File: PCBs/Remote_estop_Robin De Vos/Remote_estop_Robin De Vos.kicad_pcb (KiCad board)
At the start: 2 copper layers, 52 x 43.5 mm, 22 parts, among them J1 UART connector, J2 USB_B_Micro, SW1 SW_Push, SW2 SW_Push, SW3 SW_Push, U1 ESP32-WROOM-32E, U2 AMS1117-3.3

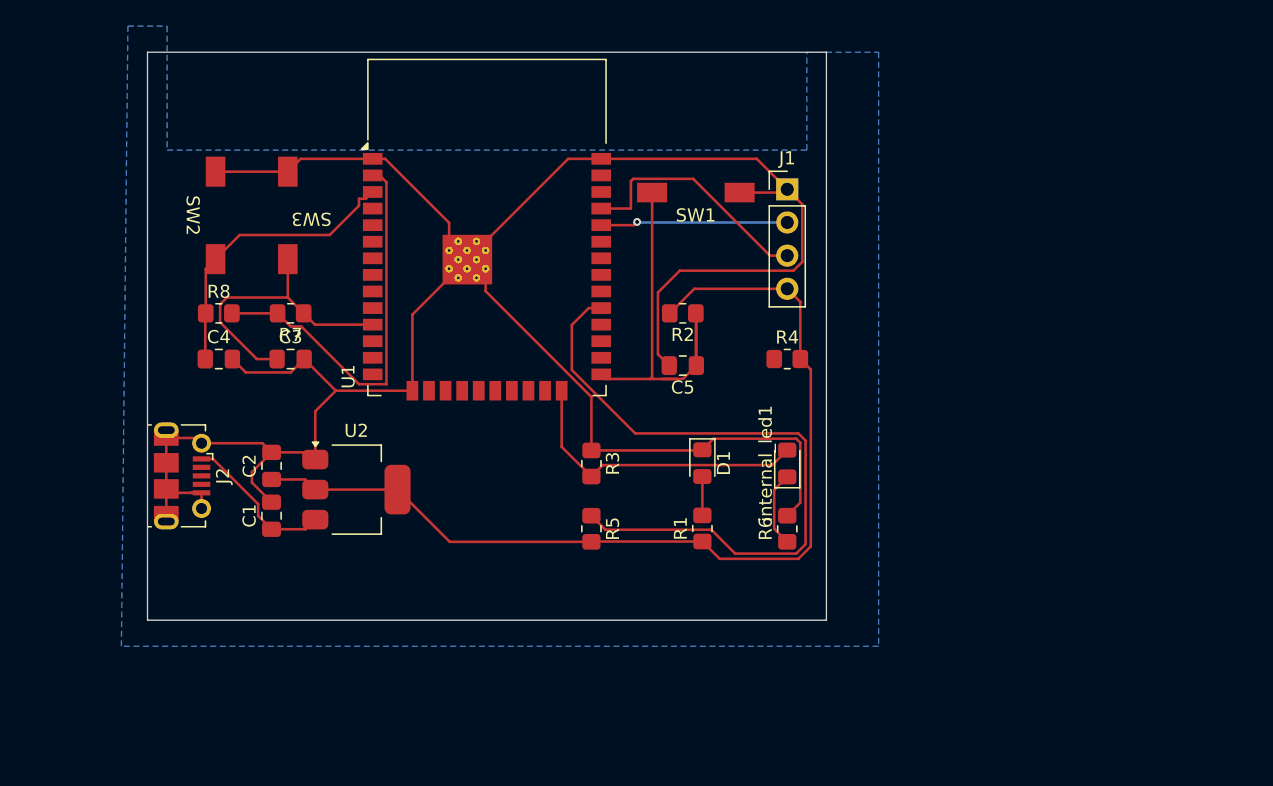
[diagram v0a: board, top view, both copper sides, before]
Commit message: pcb remote estop v2
Versie 2 met betere routing en begin van de silkscreen
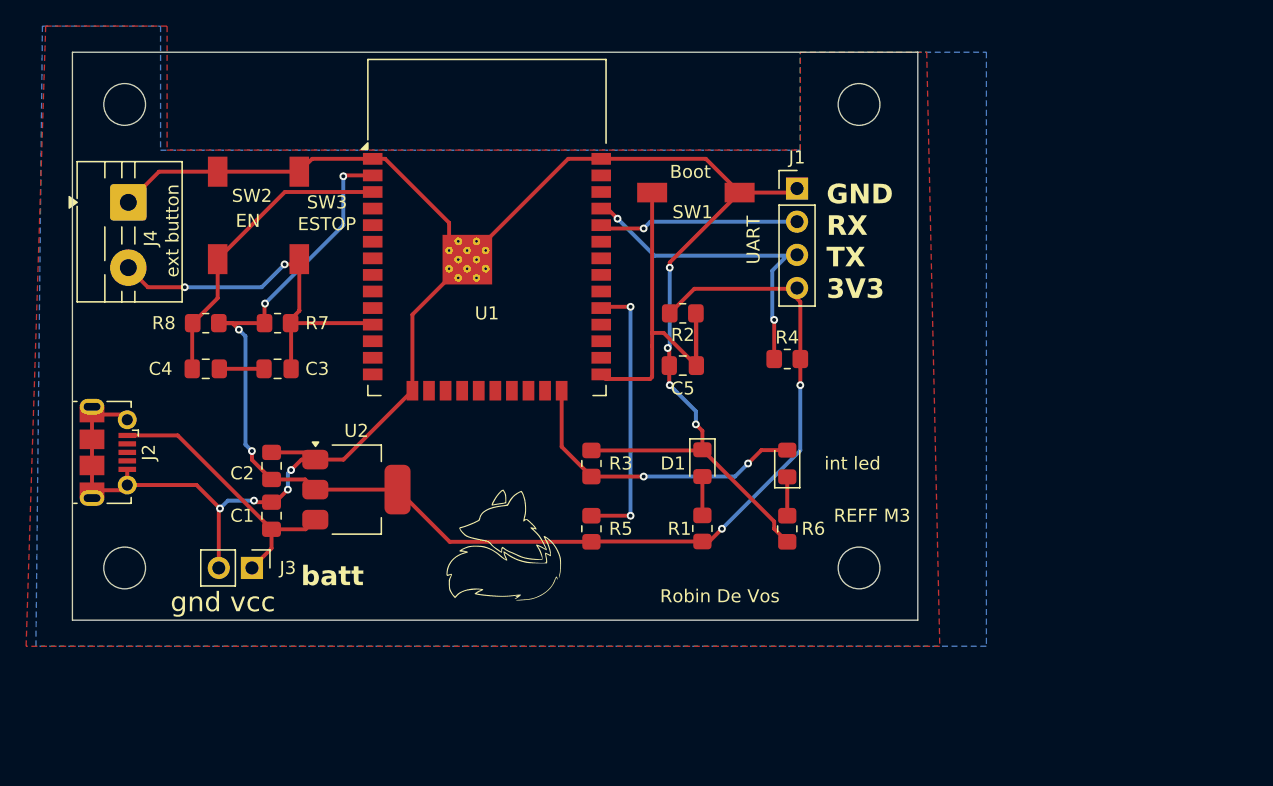
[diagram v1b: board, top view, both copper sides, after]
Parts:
- added J3: batterij connector, Connector_PinHeader_2.54mm:PinHeader_1x02_P2.54mm_Vertical, F.Cu at (105.0, 106.0)
- added J4: button bypass, TerminalBlock:TerminalBlock_MaiXu_MX126-5.0-02P_1x02_P5.00mm, F.Cu at (95.5, 78.0)
- added REF**: MountingHole_3.2mm_M3, MountingHole:MountingHole_3.2mm_M3, F.Cu at (95.2, 106.0)
- added REF**: MountingHole_3.2mm_M3, MountingHole:MountingHole_3.2mm_M3, F.Cu at (151.5, 70.5)
- added REF**: MountingHole_3.2mm_M3, MountingHole:MountingHole_3.2mm_M3, F.Cu at (95.2, 70.5)
- added REFF M3: MountingHole_3.2mm_M3, MountingHole:MountingHole_3.2mm_M3, F.Cu at (151.5, 106.0)
- int led: renamed from internal_led1
- moved J2 5.97 mm to (94.0, 97.2)
- moved C3 1.25 mm to (107.0, 90.8), turned to 180 degrees
- moved C4 1.25 mm to (101.5, 90.8)
- moved R7 1.25 mm to (107.0, 87.2)
- moved R8 1.25 mm to (101.5, 87.2)
- moved SW3 0.88 mm to (110.9, 79.0)
- moved J1 0.75 mm to (146.8, 76.9)
- moved SW2 0.16 mm to (100.1, 79.0)
- turned R6 to -90 degrees
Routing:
- net Net-(U1-IO5): track 52.2 -> 21.3 mm, vias 0 -> 2
- net GND: track 175.4 -> 160.1 mm, vias 0 -> 8
- net VCC: track 11.8 -> 21.3 mm
- net Net-(J4-Pin_2): track 22.6 -> 29.6 mm, vias 0 -> 2
- net Net-(J1-Pin_3): track 18.9 -> 24.3 mm, vias 0 -> 2
- net +3V3: track 105.4 -> 102.3 mm, vias 0 -> 6
- net Net-(internal_led1-K): track 5.80 -> 2.97 mm
- net Net-(J1-Pin_2): track 14.7 -> 15.8 mm
- net Net-(U1-EN): track 22.5 -> 23.2 mm
- net Net-(U1-IO0): track 30.9 -> 30.2 mm
- net Net-(U1-IO2): vias 0 -> 2
- added copper zone on F.Cu, net GND
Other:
- board size 52 x 43.5 mm -> 64.8 x 43.5 mm
- board text added: "Boot"
- board text added: "EN"
- board text added: "ESTOP"
- board text added: "GND RX TX 3V3"
- board text added: "Robin De Vos"
- board text added: "UART"
- board text added: "batt"
- board text added: "ext button"
- board text added: "gnd vcc"

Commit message: pcb remote estop v2
pcb Voldoet nu aan de DRC met slechts 1 warning namelijk dat esp footprint niet meer overeen komt met de library doordat de via grootte moest worden aangepast.
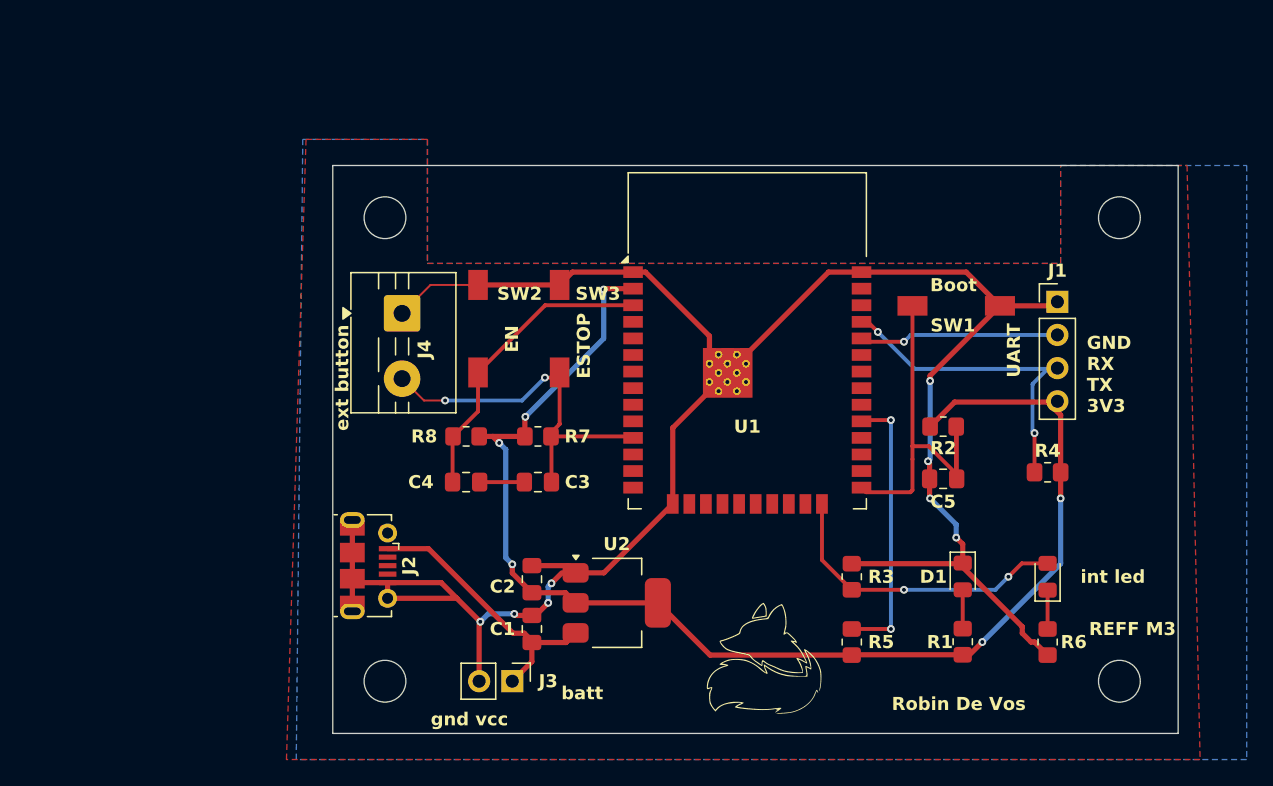
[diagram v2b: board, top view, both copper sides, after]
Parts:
- moved J4 22.6 mm to (116.5, 86.5)
- moved C2 21.7 mm to (126.4, 106.9)
- moved D1 21.7 mm to (159.4, 106.7)
- moved R1 21.7 mm to (159.4, 111.7)
- moved C1 21.7 mm to (126.4, 110.7)
- moved C3 21.7 mm to (126.9, 99.4)
- moved C4 21.7 mm to (121.4, 99.4)
- moved C5 21.7 mm to (157.9, 99.2)
- moved J1 21.7 mm to (166.7, 85.6)
- moved J2 21.7 mm to (113.9, 105.8)
- moved J3 21.7 mm to (124.9, 114.7)
- moved R2 21.7 mm to (157.9, 95.2)
- moved R3 21.7 mm to (150.9, 106.7)
- moved R4 21.7 mm to (165.9, 98.7)
- moved R5 21.7 mm to (150.9, 111.7)
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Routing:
- net GND: track 160.1 -> 163.2 mm
- net Net-(J4-Pin_2): track 29.6 -> 28.7 mm

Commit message: pcb remote estop v3
 kleine fout met marges voor knoppen gefixd drc is nu ook opnieuw goed
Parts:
- int_led1: renamed from int led
- moved SW2 3.45 mm to (123.5, 88.0)
- moved SW1 2.22 mm to (158.5, 86.0)
- moved SW3 1.35 mm to (129.5, 88.0)
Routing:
- net GND: track 163.2 -> 145.8 mm
- net Net-(U1-EN): track 23.2 -> 22.0 mm, vias 0 -> 2
- net Net-(J4-Pin_2): track 28.7 -> 27.8 mm
- net Net-(J1-Pin_3): track 24.3 -> 24.9 mm
- net +3V3: track 102.3 -> 101.7 mm
- net Net-(U1-IO0): track 30.4 -> 30.8 mm, vias 0 -> 2
- net Net-(J1-Pin_2): track 15.8 -> 15.9 mm, vias 1 -> 0

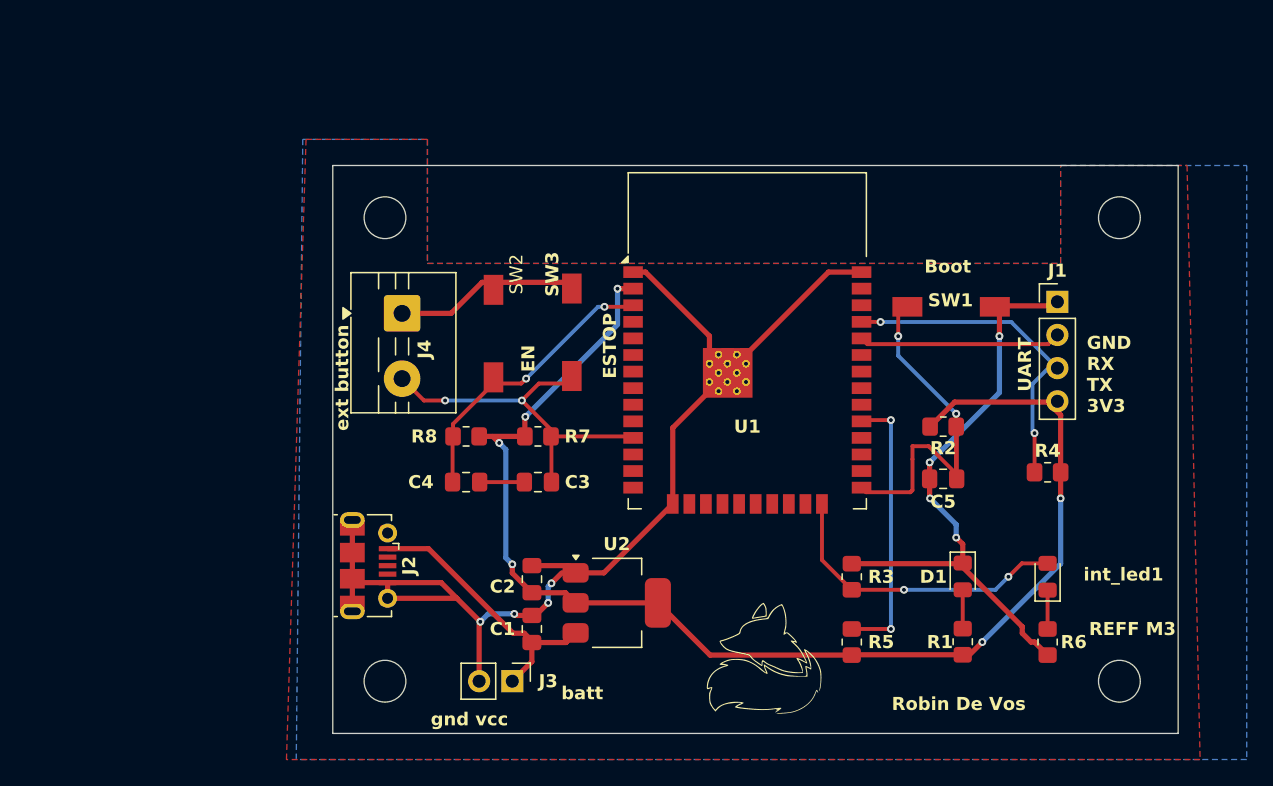
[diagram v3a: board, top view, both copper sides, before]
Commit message: pcb remote estop v4
finale versie volledig in orde me de commentaren van de prof
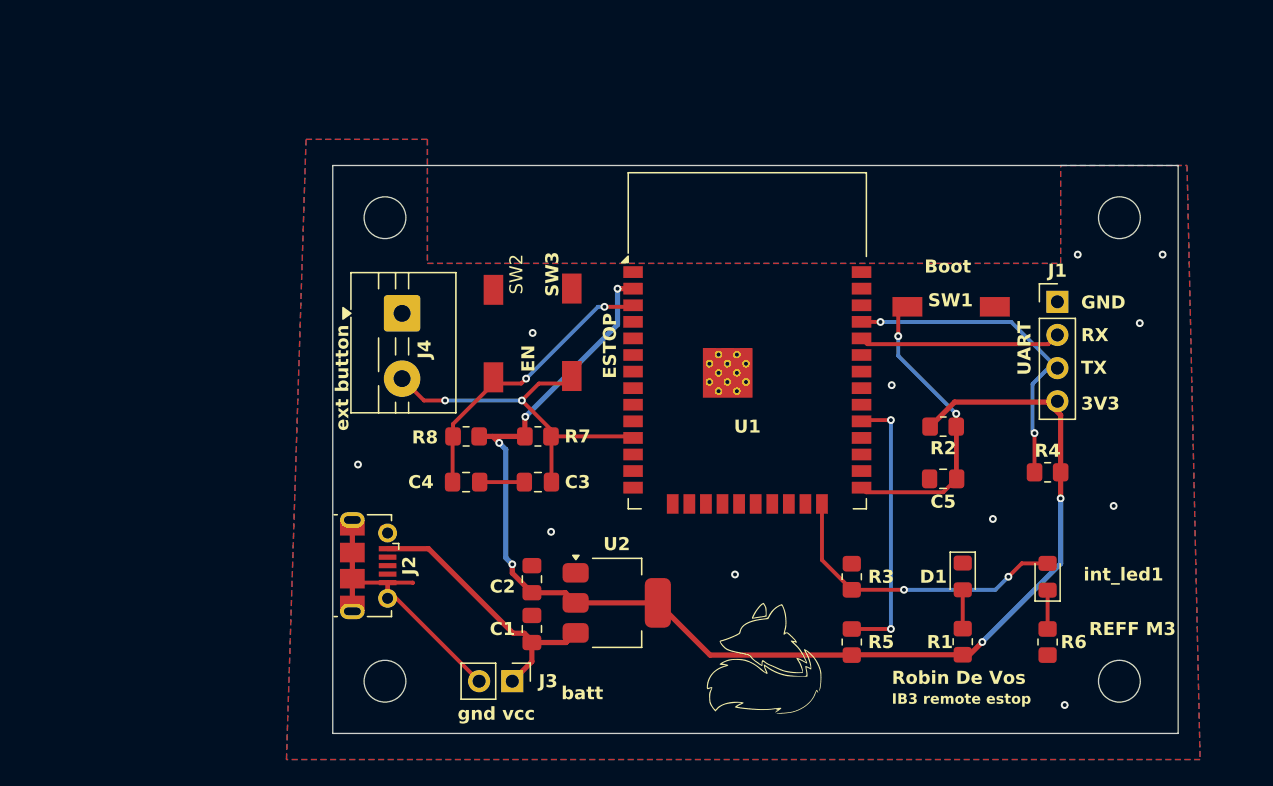
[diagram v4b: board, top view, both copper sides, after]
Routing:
- net GND: track 145.8 -> 29.3 mm, vias 8 -> 11
- net Net-(U1-IO0): track 30.8 -> 26.9 mm
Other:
- board text added: "3V3"
- board text added: "GND"
- board text added: "IB3 remote estop"
- board text added: "RX"
- board text added: "TX"
- board text added: "pin 11"
- board text removed: "GND RX TX 3V3"
